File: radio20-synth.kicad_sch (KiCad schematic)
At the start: 0 parts

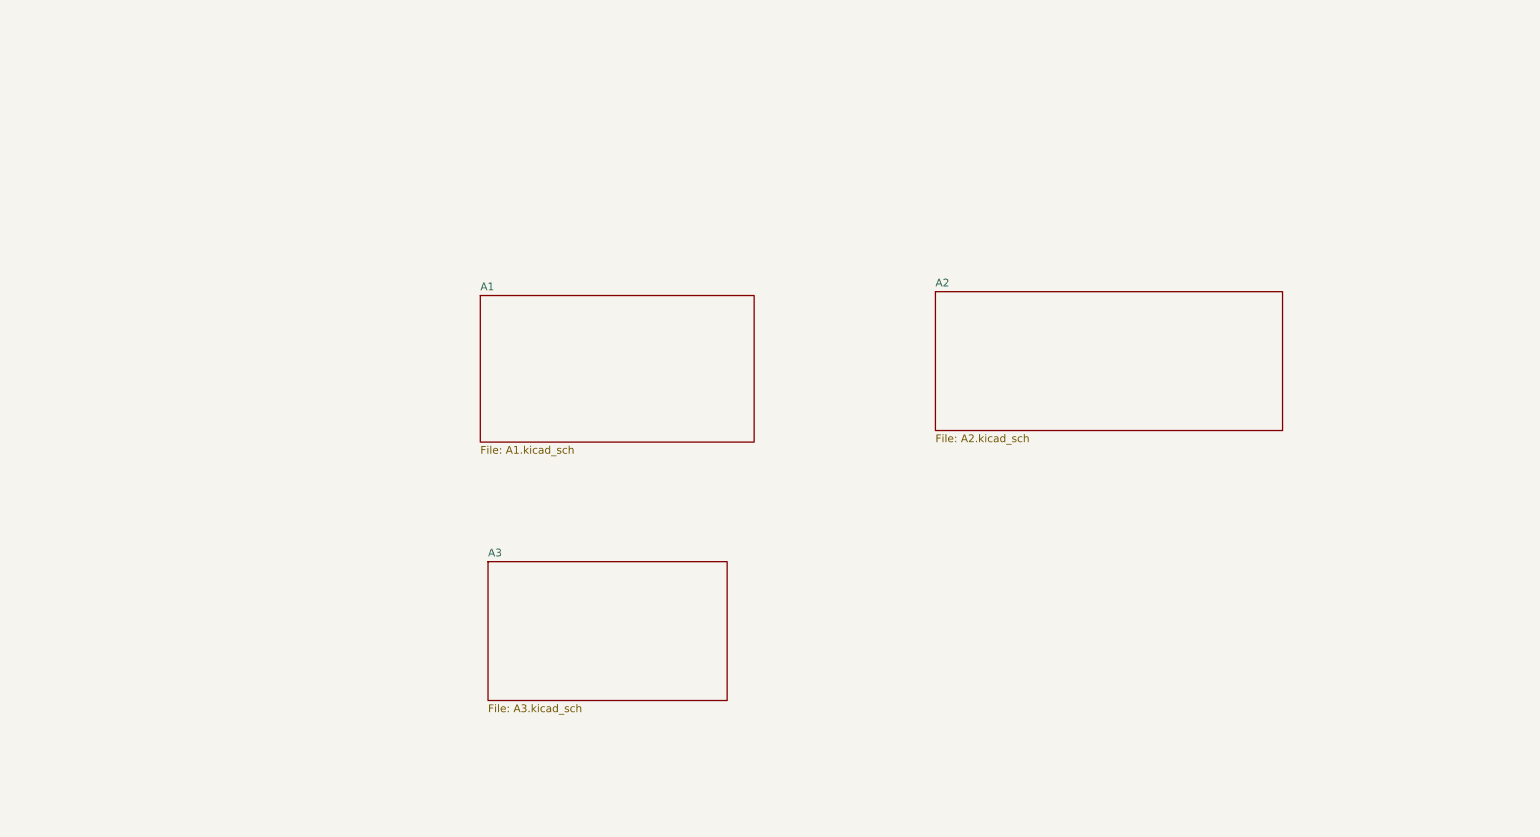
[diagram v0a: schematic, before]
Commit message: sch: adjust blocks; add freq table
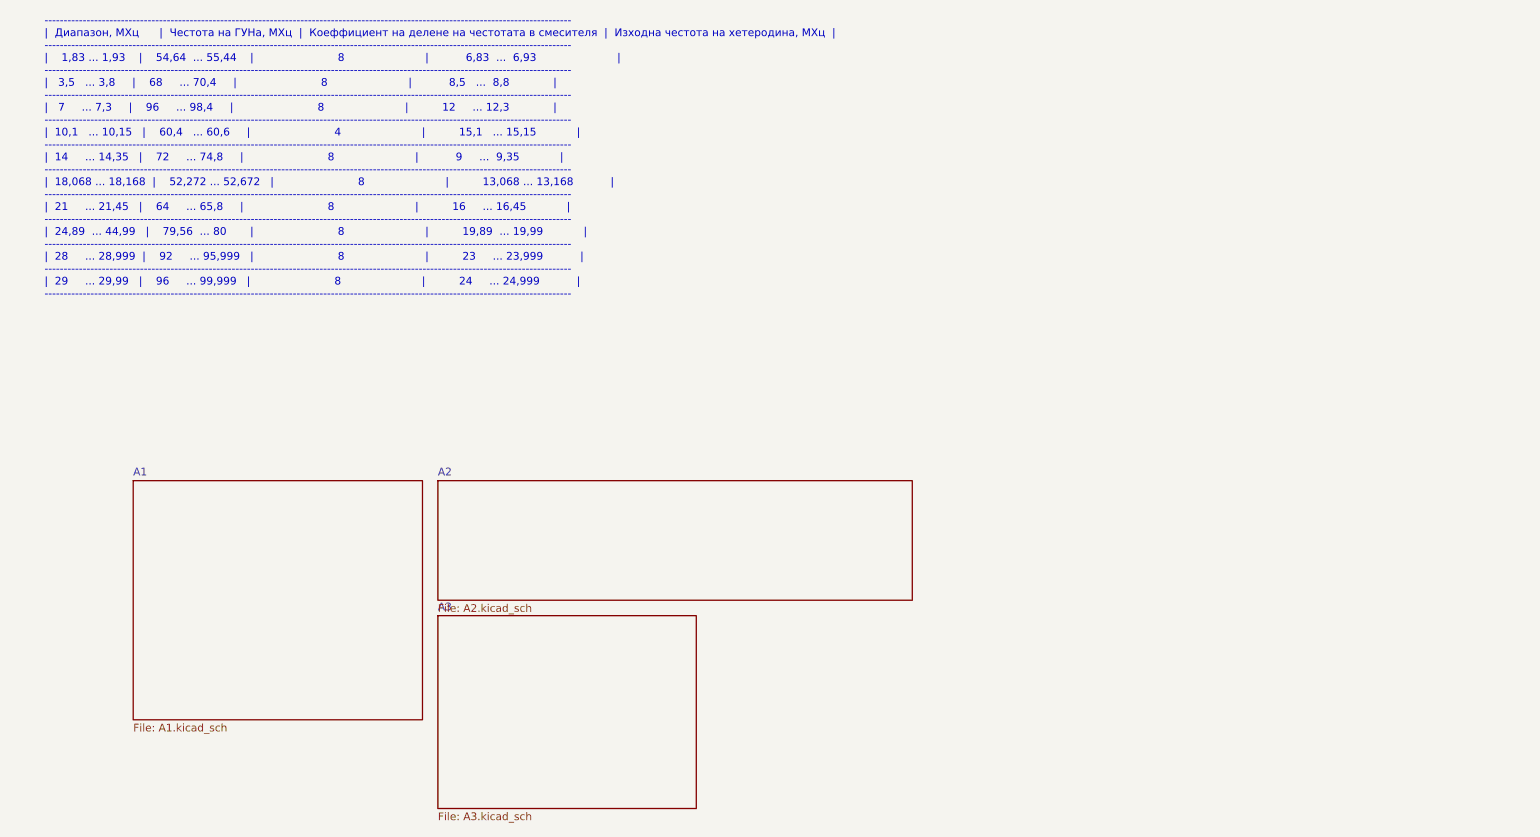
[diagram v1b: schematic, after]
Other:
- note added: "------------------------------------------------------------------------------------------------------------------------------------------ | Диапазон, МХц | Честота на ГУНа, МХц | Коеффициент на делене на честотата в смесителя | Изходна честота на хетеродина, МХц | -------------------------------------------------------------------------------------------------------------------------------------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"
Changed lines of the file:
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@@
     (title "Синтезатор на честота, Радио/1990/1,2,3")
   )
-  (sheet (at 100.965 111.76) (size 39.37 22.86) (fields_autoplaced)
+  (text "------------------------------------------------------------------------------------------------------------------------------------------\n|  Диапазон, МХц      |  Честота на ГУНа, МХц  |  Коеффициент на делене на честотата в смесителя  |  Изходна честота на хетеродина, МХц  |\n------------------------------------------------------------------------------------------------------------------------------------------\n|    1,83 ... 1,93    |    54,64  ... 55,44    |                         8                        |           6,83  ...  6,93                        |\n------------------------------------------------------------------------------------------------------------------------------------------\n|   3,5   ... 3,8     |    68     ... 70,4     |                         8                        |           8,5   ...  8,8             |\n------------------------------------------------------------------------------------------------------------------------------------------\n|   7     ... 7,3     |    96     ... 98,4     |                         8                        |          12     ... 12,3             |\n------------------------------------------------------------------------------------------------------------------------------------------\n|  10,1   ... 10,15   |    60,4   ... 60,6     |                         4                        |          15,1   ... 15,15            |\n------------------------------------------------------------------------------------------------------------------------------------------\n|  14     ... 14,35   |    72     ... 74,8     |                         8                        |           9     ...  9,35            |\n------------------------------------------------------------------------------------------------------------------------------------------\n|  18,068 ... 18,168  |    52,272 ... 52,672   |                         8                        |          13,068 ... 13,168           |\n------------------------------------------------------------------------------------------------------------------------------------------\n|  21     ... 21,45   |    64     ... 65,8     |                         8                        |          16     ... 16,45            |\n------------------------------------------------------------------------------------------------------------------------------------------\n|  24,89  ... 44,99   |    79,56  ... 80       |                         8                        |          19,89  ... 19,99            |\n------------------------------------------------------------------------------------------------------------------------------------------\n|  28     ... 28,999  |    92     ... 95,999   |                         8                        |          23     ... 23,999           |\n------------------------------------------------------------------------------------------------------------------------------------------\n|  29     ... 29,99   |    96     ... 99,999   |                         8                        |          24     ... 24,999           |\n------------------------------------------------------------------------------------------------------------------------------------------\n"
+    (at 27.94 68.58 0)
+    (effects (font (size 1.27 1.27)) (justify left bottom))
+  )
+  (sheet (at 92.71 120.65) (size 42.545 31.75) (fields_autoplaced)
     (stroke (width 0.1524) (type solid) (color 0 0 0 0))
     (fill (color 0 0 0 0.0000))
-    (property "Sheet name" "A3" (id 0) (at 100.965 111.0484 0)
+    (property "Sheet name" "A3" (id 0) (at 92.71 119.9384 0)
       (effects (font (size 1.27 1.27)) (justify left bottom))
     )
-    (property "Sheet file" "A3.kicad_sch" (id 1) (at 100.965 135.2046 0)
+    (property "Sheet file" "A3.kicad_sch" (id 1) (at 92.71 152.9846 0)
       (effects (font (size 1.27 1.27)) (justify left top))
     )
   )
-  (sheet (at 174.625 67.31) (size 57.15 22.86) (fields_autoplaced)
+  (sheet (at 92.71 98.425) (size 78.105 19.685) (fields_autoplaced)
     (stroke (width 0.1524) (type solid) (color 0 0 0 0))
     (fill (color 0 0 0 0.0000))
-    (property "Sheet name" "A2" (id 0) (at 174.625 66.5984 0)
+    (property "Sheet name" "A2" (id 0) (at 92.71 97.7134 0)
       (effects (font (size 1.27 1.27)) (justify left bottom))
     )
-    (property "Sheet file" "A2.kicad_sch" (id 1) (at 174.625 90.7546 0)
+    (property "Sheet file" "A2.kicad_sch" (id 1) (at 92.71 118.6946 0)
       (effects (font (size 1.27 1.27)) (justify left top))
     )
   )
-  (sheet (at 99.695 67.945) (size 45.085 24.13) (fields_autoplaced)
+  (sheet (at 42.545 98.425) (size 47.625 39.37) (fields_autoplaced)
     (stroke (width 0.1524) (type solid) (color 0 0 0 0))
     (fill (color 0 0 0 0.0000))
-    (property "Sheet name" "A1" (id 0) (at 99.695 67.2334 0)
+    (property "Sheet name" "A1" (id 0) (at 42.545 97.7134 0)
       (effects (font (size 1.27 1.27)) (justify left bottom))
     )
-    (property "Sheet file" "A1.kicad_sch" (id 1) (at 99.695 92.6596 0)
+    (property "Sheet file" "A1.kicad_sch" (id 1) (at 42.545 138.3796 0)
       (effects (font (size 1.27 1.27)) (justify left top))
     )

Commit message: sch: Fix typo in freq table; adjust formatting
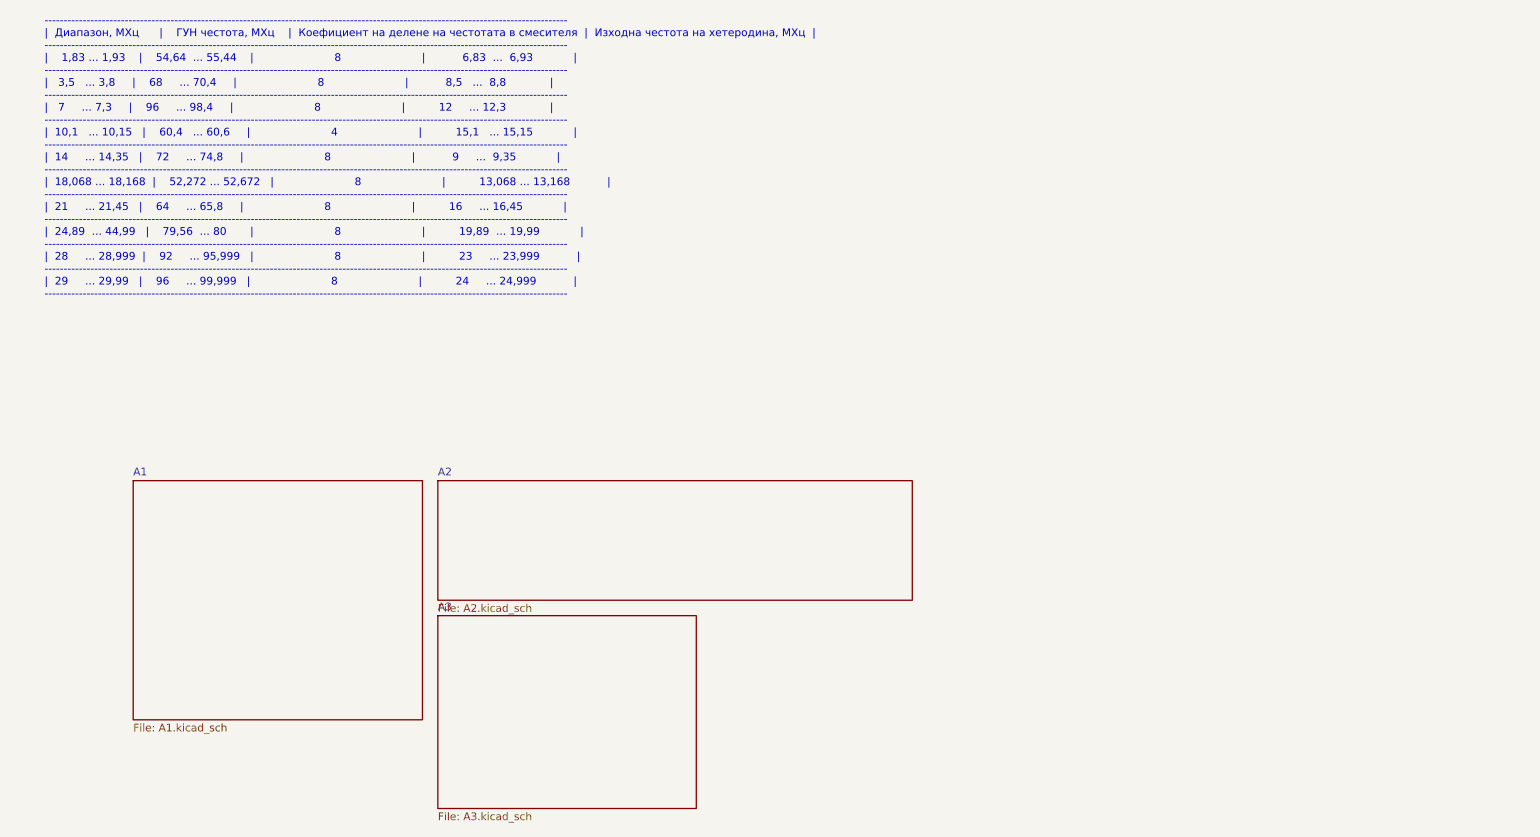
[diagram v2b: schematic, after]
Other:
- note added: "----------------------------------------------------------------------------------------------------------------------------------------- | Диапазон, МХц | ГУН честота, МХц | Коефициент на делене на честотата в смесителя | Изходна честота на хетеродина, МХц | ----------------------------------------------------------------------------------------------------------------------------------------- |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"
- note removed: "------------------------------------------------------------------------------------------------------------------------------------------ | Диапазон, МХц | Честота на ГУНа, МХц | Коеффициент на делене на честотата в смесителя | Изходна честота на хетеродина, МХц | -------------------------------------------------------------------------------------------------------------------------------------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"
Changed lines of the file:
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@@
     (title "Синтезатор на честота, Радио/1990/1,2,3")
   )
-  (text "------------------------------------------------------------------------------------------------------------------------------------------\n|  Диапазон, МХц      |  Честота на ГУНа, МХц  |  Коеффициент на делене на честотата в смесителя  |  Изходна честота на хетеродина, МХц  |\n------------------------------------------------------------------------------------------------------------------------------------------\n|    1,83 ... 1,93    |    54,64  ... 55,44    |                         8                        |           6,83  ...  6,93                        |\n------------------------------------------------------------------------------------------------------------------------------------------\n|   3,5   ... 3,8     |    68     ... 70,4     |                         8                        |           8,5   ...  8,8             |\n------------------------------------------------------------------------------------------------------------------------------------------\n|   7     ... 7,3     |    96     ... 98,4     |                         8                        |          12     ... 12,3             |\n------------------------------------------------------------------------------------------------------------------------------------------\n|  10,1   ... 10,15   |    60,4   ... 60,6     |                         4                        |          15,1   ... 15,15            |\n------------------------------------------------------------------------------------------------------------------------------------------\n|  14     ... 14,35   |    72     ... 74,8     |                         8                        |           9     ...  9,35            |\n------------------------------------------------------------------------------------------------------------------------------------------\n|  18,068 ... 18,168  |    52,272 ... 52,672   |                         8                        |          13,068 ... 13,168           |\n------------------------------------------------------------------------------------------------------------------------------------------\n|  21     ... 21,45   |    64     ... 65,8     |                         8                        |          16     ... 16,45            |\n------------------------------------------------------------------------------------------------------------------------------------------\n|  24,89  ... 44,99   |    79,56  ... 80       |                         8                        |          19,89  ... 19,99            |\n------------------------------------------------------------------------------------------------------------------------------------------\n|  28     ... 28,999  |    92     ... 95,999   |                         8                        |          23     ... 23,999           |\n------------------------------------------------------------------------------------------------------------------------------------------\n|  29     ... 29,99   |    96     ... 99,999   |                         8                        |          24     ... 24,999           |\n------------------------------------------------------------------------------------------------------------------------------------------\n"
+  (text "-----------------------------------------------------------------------------------------------------------------------------------------\n|  Диапазон, МХц      |    ГУН честота, МХц    |  Коефициент на делене на честотата в смесителя  |  Изходна честота на хетеродина, МХц  |\n-----------------------------------------------------------------------------------------------------------------------------------------\n|    1,83 ... 1,93    |    54,64  ... 55,44    |                        8                        |           6,83  ...  6,93            |\n-----------------------------------------------------------------------------------------------------------------------------------------\n|   3,5   ... 3,8     |    68     ... 70,4     |                        8                        |           8,5   ...  8,8             |\n-----------------------------------------------------------------------------------------------------------------------------------------\n|   7     ... 7,3     |    96     ... 98,4     |                        8                        |          12     ... 12,3             |\n-----------------------------------------------------------------------------------------------------------------------------------------\n|  10,1   ... 10,15   |    60,4   ... 60,6     |                        4                        |          15,1   ... 15,15            |\n-----------------------------------------------------------------------------------------------------------------------------------------\n|  14     ... 14,35   |    72     ... 74,8     |                        8                        |           9     ...  9,35            |\n-----------------------------------------------------------------------------------------------------------------------------------------\n|  18,068 ... 18,168  |    52,272 ... 52,672   |                        8                        |          13,068 ... 13,168           |\n-----------------------------------------------------------------------------------------------------------------------------------------\n|  21     ... 21,45   |    64     ... 65,8     |                        8                        |          16     ... 16,45            |\n-----------------------------------------------------------------------------------------------------------------------------------------\n|  24,89  ... 44,99   |    79,56  ... 80       |                        8                        |          19,89  ... 19,99            |\n-----------------------------------------------------------------------------------------------------------------------------------------\n|  28     ... 28,999  |    92     ... 95,999   |                        8                        |          23     ... 23,999           |\n-----------------------------------------------------------------------------------------------------------------------------------------\n|  29     ... 29,99   |    96     ... 99,999   |                        8                        |          24     ... 24,999           |\n-----------------------------------------------------------------------------------------------------------------------------------------\n"
     (at 27.94 68.58 0)
     (effects (font (size 1.27 1.27)) (justify left bottom))
